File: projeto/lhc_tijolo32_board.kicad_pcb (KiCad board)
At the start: 2 copper layers, 25.4 x 64.8 mm, 49 parts, among them J1 USB_C_Receptacle_USB2.0, J2 OLED, J3 JTAG 10pin Connector, J4 Conn_01x20_Male, Q1 MMBT3904, Q2 MMBT3904, SW1 SW_Push, SW2 SW_Push, U1 AMS1117-3.3, U2 CH340G, U3 ESP32-WROOM-32D, Y1 12MHz 10ppm, Y2 32k 20ppm

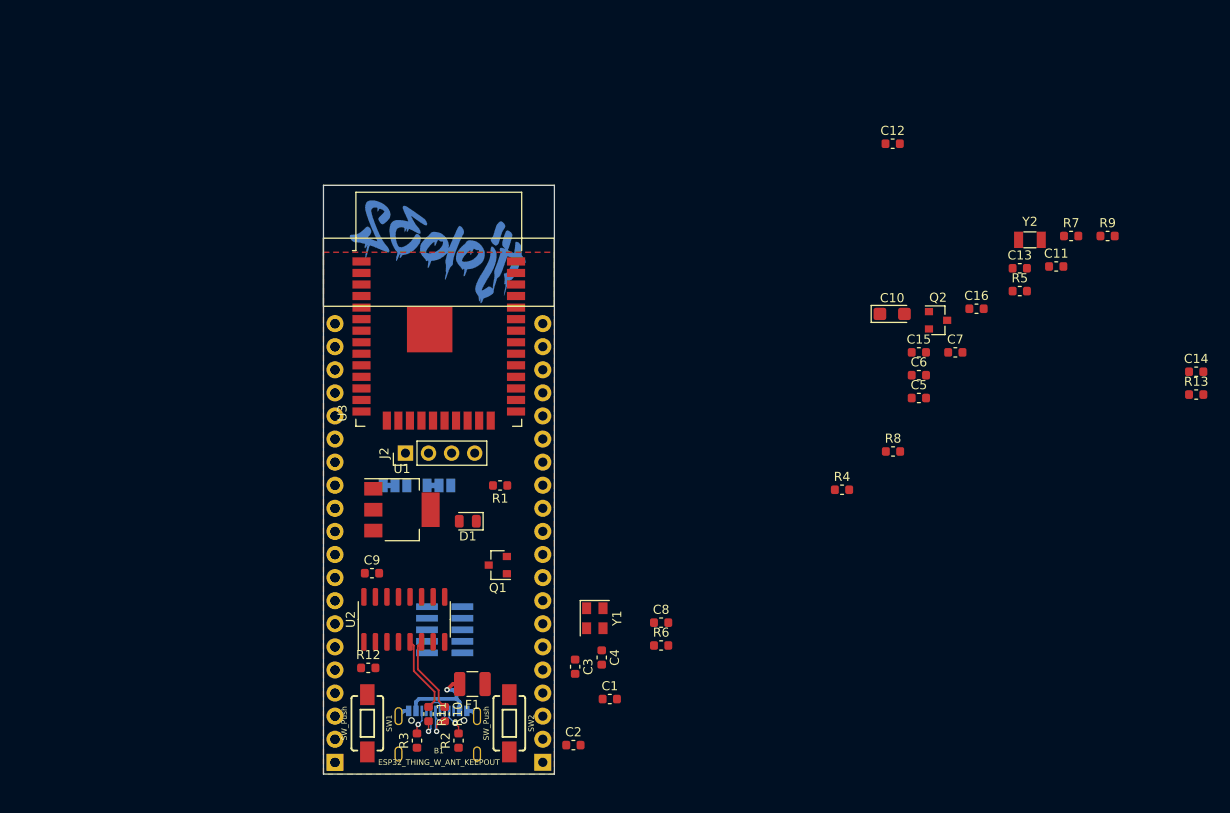
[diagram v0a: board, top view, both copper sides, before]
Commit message: Changed from Sparkfun to Adafruit Feather layout
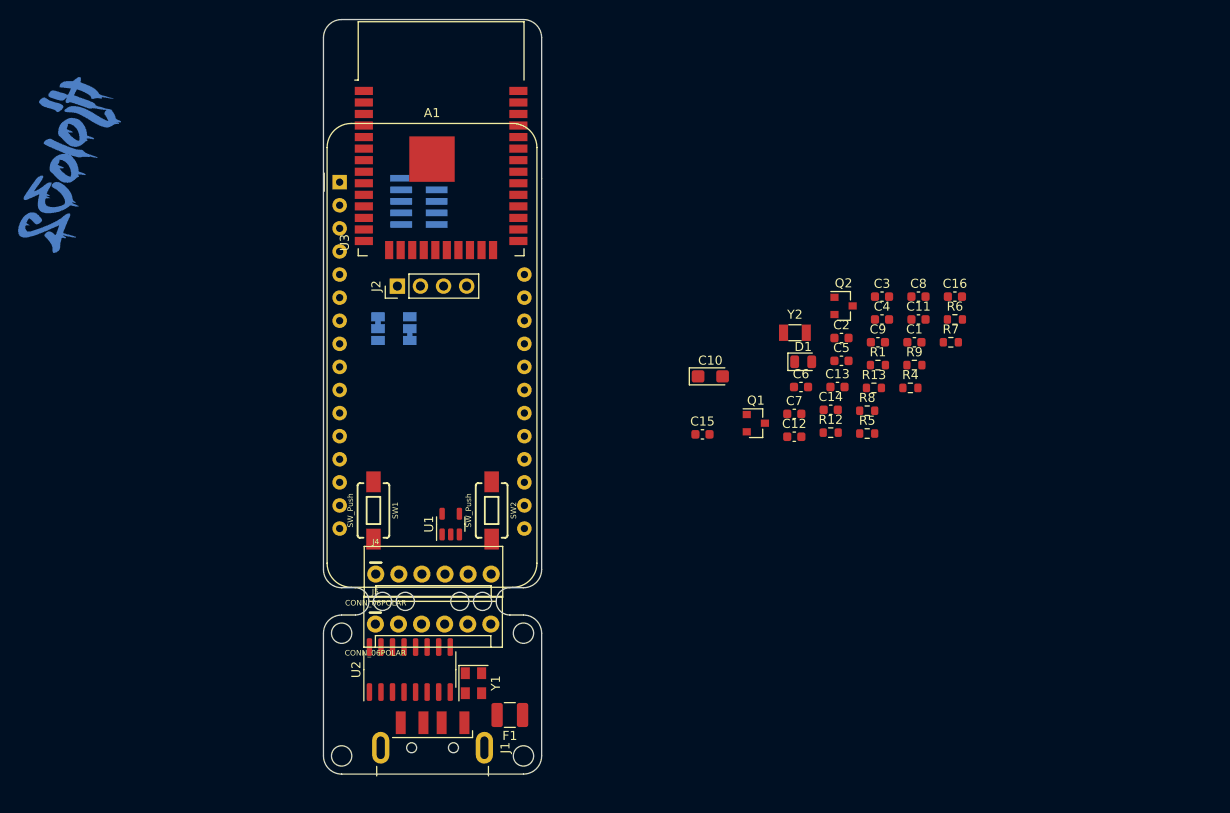
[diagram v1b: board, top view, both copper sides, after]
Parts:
- removed B1: ESP32_THING_W_ANT_KEEPOUT, Boards:ESP32_THING
- removed R10, R11: 0R, Resistor_SMD:R_0603_1608Metric
- removed R2, R3: 5k1R, Resistor_SMD:R_0603_1608Metric
- added A1: Adafruit_Feather_Generic, Module:Adafruit_Feather, F.Cu at (103.4, 45.4)
- added J5: CONN_06POLAR, Connectors:MOLEX-1X6, F.Cu at (107.3, 94.0)
- J1: value USB_C_Receptacle_USB2.0 -> USB_A; footprint Connector_USB:USB_C_Receptacle_Palconn_UTC16-G -> Connector_USB:USB_A_CNCTech_1001-011-01101_Horizontal; moved to F.Cu
- J4: value Conn_01x20_Male -> CONN_06POLAR; footprint Connector_PinHeader_2.54mm:PinHeader_1x20_P2.54mm_Vertical -> Connectors:MOLEX-1X6; moved to F.Cu
- U1: value AMS1117-3.3 -> AP2112K-3.3; footprint Package_TO_SOT_SMD:SOT-223-3_TabPin2 -> Package_TO_SOT_SMD:SOT-23-5
- moved C9 61.2 mm to (162.6, 63.0)
- moved R12 57.1 mm to (157.4, 72.9)
- moved C2 53.6 mm to (158.6, 62.5)
- moved C3 52.9 mm to (163.0, 58.0), turned to 0 degrees
- moved C1 51.6 mm to (166.6, 63.0)
- moved C4 48.3 mm to (163.0, 60.5), turned to 0 degrees
- moved R6 48.3 mm to (171.1, 60.5)
- moved J3 47.2 mm to (112.1, 47.5), turned to 180 degrees
- moved C8 45.7 mm to (167.1, 58.0)
- moved R1 43.6 mm to (162.6, 65.5), turned to 0 degrees
- moved G*** 41.7 mm to (73.6, 43.5), turned to 270 degrees (x2)
- moved D1 40.9 mm to (154.4, 65.1), turned to 0 degrees
- moved C14 40.4 mm to (157.4, 70.4)
- moved R13 35.5 mm to (162.2, 68.0)
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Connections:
- J4 pad 1: Net-(J4-Pad1) -> 5V
- J4 pad 2: Net-(J4-Pad2) -> ESP_RX
- J4 pad 3: Net-(J4-Pad3) -> ESP_TX
- J4 pad 4: Net-(J4-Pad4) -> DTR
- J4 pad 5: Net-(J4-Pad5) -> RTS
- J4 pad 6: Net-(J4-Pad6) -> GND
- U1 pad 1: GND -> 5V
- U1 pad 2: +3V3 -> GND
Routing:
- net Net-(F1-Pad2): track 10.5 -> 0.00 mm, vias 1 -> 0
- net D-: track 8.54 -> 0.00 mm
- net D+: track 8.54 -> 0.00 mm
- net Net-(J1-PadA7): track 6.75 -> 0.00 mm, vias 1 -> 0
- net Net-(J1-PadA6): track 6.10 -> 0.00 mm, vias 1 -> 0
- net Net-(J1-PadA5): track 2.93 -> 0.00 mm, vias 1 -> 0
- net GND: track 2.72 -> 0.00 mm
- net Net-(J1-PadB5): track 2.71 -> 0.00 mm, vias 1 -> 0
- removed copper zone on F.Cu, net GND
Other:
- board size 25.4 x 64.8 mm -> 24 x 83 mm

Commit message: Layout updated and added new 3d images
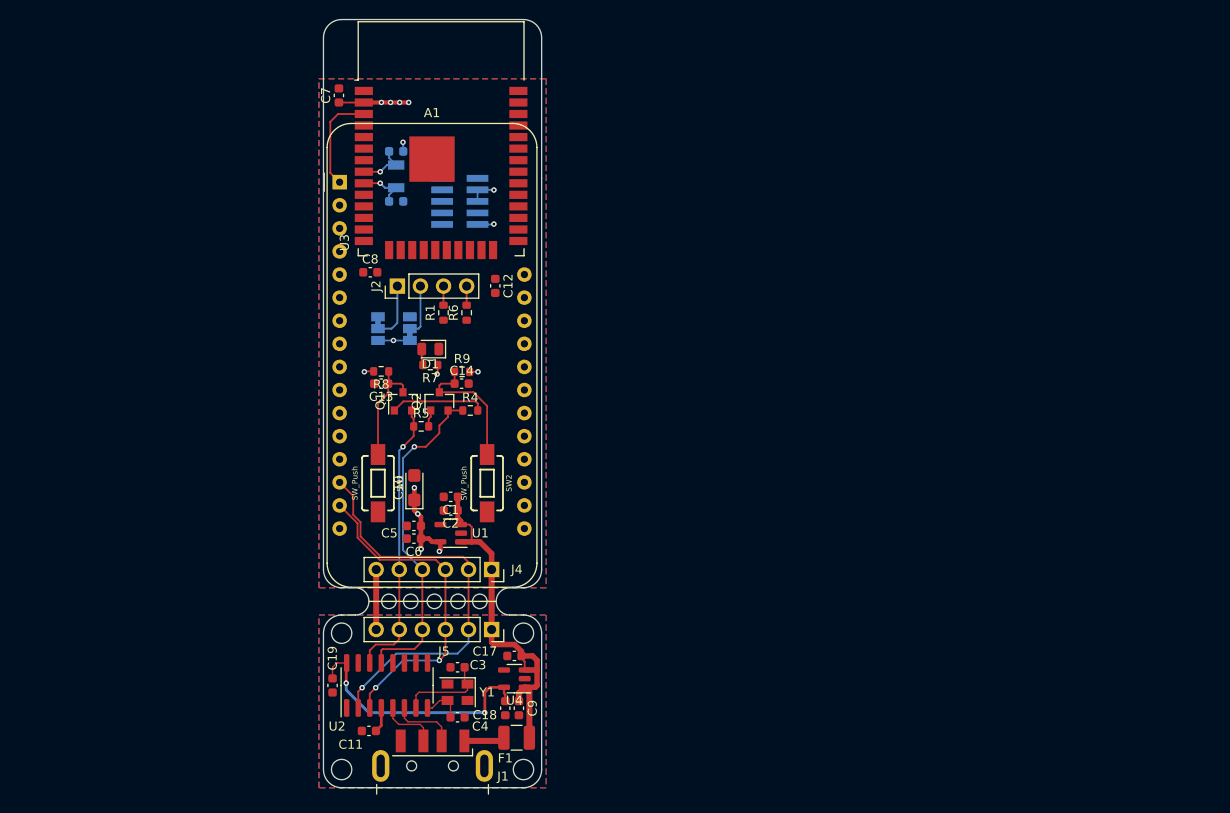
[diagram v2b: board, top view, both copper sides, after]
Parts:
- removed G***: LOGO, lhc_logos:tijolo32_medium_mask
- removed G***: LOGO, lhc_logos:tijolo32_medium_cu
- removed R12, R13: 0R, Resistor_SMD:R_0603_1608Metric
- added C17: 100nF, Capacitor_SMD:C_0603_1608Metric, F.Cu at (122.6, 97.5)
- added C18: 1uF, Capacitor_SMD:C_0603_1608Metric, F.Cu at (121.6, 103.2)
- added C19: 100nF, Capacitor_SMD:C_0603_1608Metric, F.Cu at (102.6, 100.7)
- added U4: AP2112K-3.3, Package_TO_SOT_SMD:SOT-23-5, F.Cu at (122.6, 100.0)
- C15, C16, Y2: moved to B.Cu
- C9: value 100nF -> 1uF
- J4, J5: footprint Connectors:MOLEX-1X6 -> Connector_PinSocket_2.54mm:PinSocket_1x06_P2.54mm_Vertical
- moved C11 75.5 mm to (106.6, 105.7), turned to 180 degrees
- moved C4 64.0 mm to (116.3, 104.2), turned to 180 degrees
- moved C16 62.3 mm to (109.6, 47.5)
- moved C3 62.0 mm to (116.3, 98.7), turned to 180 degrees
- moved C7 61.1 mm to (103.3, 35.8), turned to 90 degrees
- moved C8 60.4 mm to (106.8, 55.3)
- moved R7 57.3 mm to (113.3, 65.5), turned to 180 degrees
- moved C9 56.4 mm to (123.1, 103.2), turned to 270 degrees
- moved C1 53.8 mm to (115.6, 80.0), turned to 180 degrees
- moved R6 53.7 mm to (117.3, 59.7), turned to 90 degrees
- moved R8 53.6 mm to (108.0, 66.2), turned to 180 degrees
- moved C5 50.4 mm to (111.5, 83.2), turned to 180 degrees
- moved C13 50.2 mm to (108.0, 67.5), turned to 180 degrees
- moved R9 49.8 mm to (116.8, 66.2)
- moved R5 49.1 mm to (112.3, 72.2)
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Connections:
- C3 pad 1: Net-(C3-Pad1) -> XI
- C4 pad 2: Net-(C4-Pad2) -> XO
- C9 pad 1: +3V3 -> 5V
- U2 pad 16: +3V3 -> Net-(C18-Pad1)
- U2 pad 2: Net-(R12-Pad2) -> ESP_RX
- U2 pad 3: Net-(R13-Pad1) -> ESP_TX
- Y1 pad 2: Net-(C4-Pad2) -> GND
- Y1 pad 4: Net-(C3-Pad1) -> GND
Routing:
- net ESP_RX: track 0.00 -> 45.0 mm, vias 0 -> 1
- net 5V: track 0.00 -> 40.7 mm
- net DTR: track 0.00 -> 37.0 mm, vias 0 -> 1
- net ESP_TX: track 0.00 -> 36.5 mm, vias 0 -> 2
- net RTS: track 0.00 -> 31.0 mm, vias 0 -> 1
- net Net-(C18-Pad1): track 0.00 -> 28.4 mm, vias 0 -> 2
- net ESP_RST: track 0.00 -> 23.2 mm
- net +3V3: track 0.00 -> 21.1 mm, vias 0 -> 11
- net GND: track 0.00 -> 16.0 mm, vias 0 -> 4
- net ESP_BOOT: track 0.00 -> 15.0 mm
- net Net-(Q1-Pad1): track 0.00 -> 10.5 mm
- net XI: track 0.00 -> 9.95 mm
- net D-: track 0.00 -> 7.17 mm
- net OLED_P1: track 0.00 -> 6.44 mm
- net D+: track 0.00 -> 6.40 mm
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- added copper zone on B.Cu, net +3V3
- added copper zone on B.Cu, net GND
- added copper zone on F.Cu, net GND
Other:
- board size 24 x 83 mm -> 24 x 84.5 mm

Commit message: Layout updated
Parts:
- moved D1 13.3 mm to (114.3, 77.0), turned to 270 degrees
- moved R7 11.8 mm to (116.1, 77.0), turned to 270 degrees
- moved JP1 5.70 mm to (116.6, 63.0), turned to 180 degrees
- moved JP2 4.51 mm to (111.8, 63.0), turned to 0 degrees
- moved C8 0.45 mm to (106.3, 55.5)
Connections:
- U3 pad 27: IO16 -> SDA
- U3 pad 28: IO17 -> SCL
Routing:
- net SVN: track 0.00 -> 32.2 mm, vias 0 -> 1
- net SVP: track 0.00 -> 31.8 mm, vias 0 -> 1
- net IO27: track 0.00 -> 30.6 mm
- net IO26: track 0.00 -> 29.8 mm
- net IO25: track 0.00 -> 27.9 mm, vias 0 -> 1
- net IO35: track 0.00 -> 26.6 mm, vias 0 -> 1
- net IO34: track 0.00 -> 22.5 mm, vias 0 -> 1
- net SCL: track 2.11 -> 18.7 mm, vias 0 -> 1
- net IO33-32kXN: track 5.59 -> 21.8 mm, vias 1 -> 2
- net IO14-MTMS: track 0.00 -> 15.1 mm, vias 0 -> 1
- net SDA: track 2.10 -> 17.1 mm, vias 0 -> 1
- net IO12-MTDI: track 0.00 -> 13.6 mm, vias 0 -> 3
- net ESP_BOOT: track 15.0 -> 28.5 mm
- net IO13-MTCK: track 0.00 -> 9.56 mm, vias 0 -> 1
- net IO15-MTDO: track 0.00 -> 8.99 mm, vias 0 -> 1
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
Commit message: Layout improved
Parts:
- added G***: LOGO, lhc_logos:lhc_logo_alt_small, B.Cu at (113.6, 103.0)
- moved C8 1.87 mm to (108.1, 54.9), turned to 180 degrees
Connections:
- A1 pad 10: SVN -> IO26
- A1 pad 11: IO25 -> Net-(A1-Pad11)
- A1 pad 12: IO26 -> Net-(A1-Pad12)
- A1 pad 13: IO27 -> Net-(A1-Pad13)
- A1 pad 16: IO23 -> Net-(A1-Pad16)
- A1 pad 20: IO4 -> IO22
- A1 pad 21: IO5 -> IO21
- A1 pad 22: IO18 -> IO19
- A1 pad 23: IO19 -> IO18
- A1 pad 24: IO21 -> IO5
- A1 pad 25: IO22 -> IO4
- A1 pad 28: Net-(A1-Pad28) -> IO23
- A1 pad 3: Net-(A1-Pad3) -> IO27
- A1 pad 5: IO32-32kXP -> SVP
- A1 pad 6: IO33-32kXN -> SVN
- A1 pad 9: SVP -> IO25
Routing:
- net ESP_TX: track 36.5 -> 85.1 mm, vias 2 -> 6
- net IO22: track 0.00 -> 40.1 mm, vias 0 -> 1
- net ESP_RST: track 23.2 -> 58.7 mm, vias 0 -> 4
- net IO21: track 0.00 -> 33.5 mm, vias 0 -> 1
- net SDA: track 17.1 -> 47.6 mm, vias 1 -> 2
- net SCL: track 18.7 -> 47.3 mm, vias 1 -> 2
- net IO19: track 0.00 -> 28.2 mm, vias 0 -> 1
- net IO2: track 0.00 -> 27.0 mm, vias 0 -> 1
- net IO27: track 30.6 -> 3.90 mm
- net 5V: track 40.7 -> 65.1 mm, vias 0 -> 4
- net IO18: track 0.00 -> 24.2 mm, vias 0 -> 1
- net IO23: track 0.00 -> 21.0 mm
- net IO5: track 0.00 -> 20.1 mm, vias 0 -> 1
- net IO33-32kXN: track 21.8 -> 5.58 mm, vias 2 -> 1
- net SVP: track 31.8 -> 17.5 mm
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
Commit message: Layout LIVE
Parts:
- removed the G*** at (113.6, 103.0)
- added ?: , Aesthetics:OSHW-LOGO-M, B.Cu at (122.7, 106.6)
- added ?: , Aesthetics:OSHW-LOGO-L, F.Cu at (108.4, 62.3)
- added G***: LOGO, lhc_logos:lhc_logo_alt_xlarge, B.Cu at (113.7, 33.5)
- added G***: LOGO, lhc_logos:lhc_logo_alt_large, B.Cu at (113.7, 100.3)
- JP1, JP2: footprint Jumper:SolderJumper-3_P1.3mm_Bridged12_Pad1.0x1.5mm_NumberLabels -> Jumper:SolderJumper-3_P1.3mm_Open_Pad1.0x1.5mm_NumberLabels
- moved JP2 0.09 mm to (111.8, 63.0)
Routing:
- net ESP_RX: track 38.7 -> 98.4 mm, vias 3 -> 5
- net ESP_TX: track 85.1 -> 92.1 mm, vias 6 -> 5
- net IO12-MTDI: track 11.4 -> 10.5 mm, vias 3 -> 1
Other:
- board text added: "3V3"
- board text added: "GND"
- board text added: "IO16"
- board text added: "IO17"
- board text added: "IO23"
- board text added: "LHC"

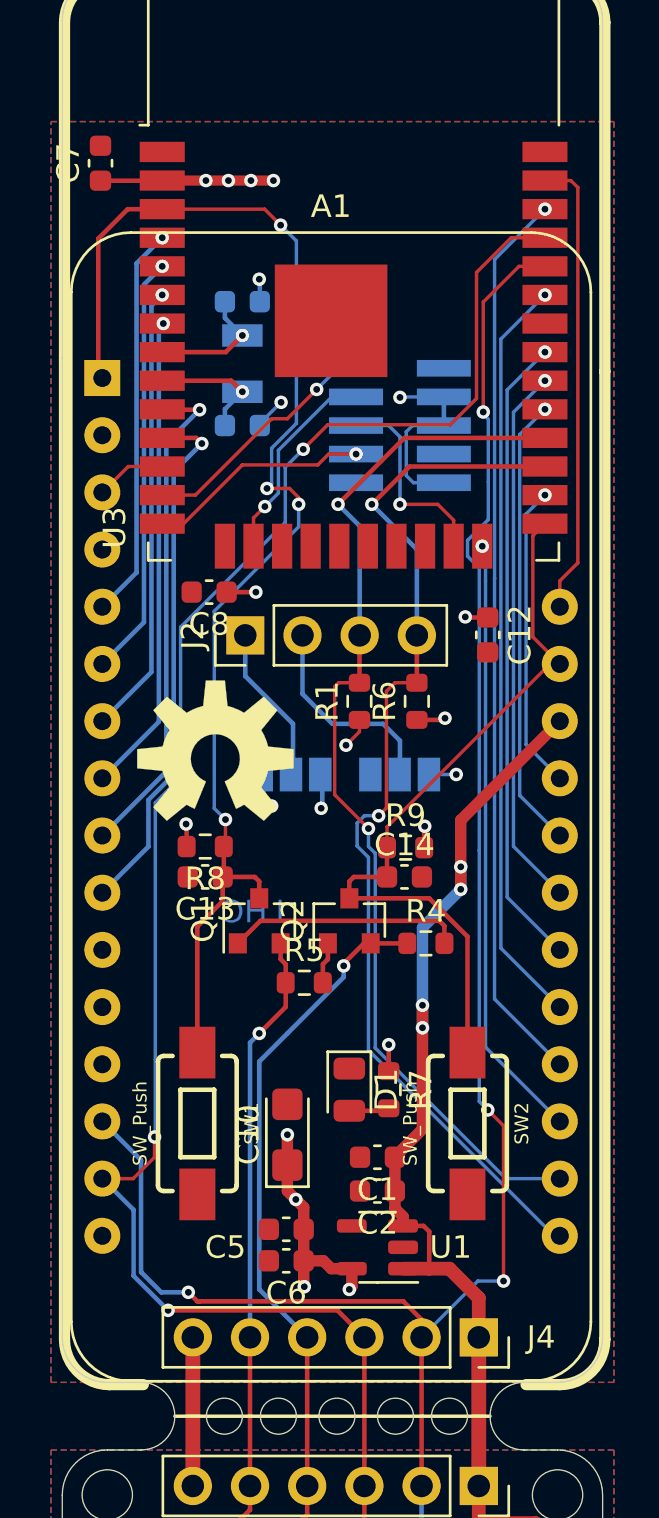
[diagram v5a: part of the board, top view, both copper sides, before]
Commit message: Updated silk on both sides
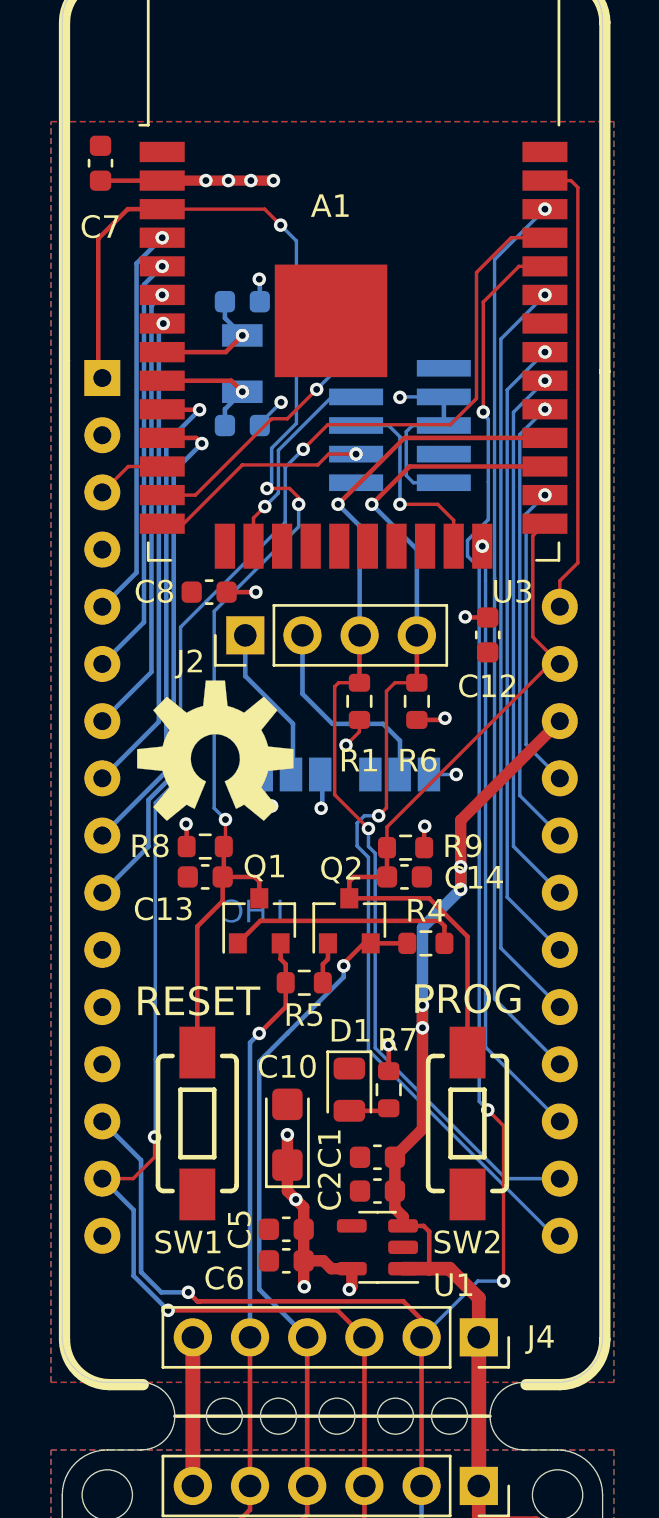
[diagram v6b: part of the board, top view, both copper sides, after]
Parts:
- removed the G*** at (113.7, 100.3)
- added G***: LOGO, lhc_logos:lhc_logo_alt_small, B.Cu at (118.0, 103.1)
- moved ? 16.2 mm to (106.9, 103.2)
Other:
- board text added: "1"
- board text added: "5V0"
- board text added: "9"
- board text added: "DEBUG"
- board text added: "DTR"
- board text added: "IO0"
- board text added: "IO02"
- board text added: "IO04"
- board text added: "IO05"
- board text added: "IO18"
- board text added: "IO19"
- board text added: "IO21"
- board text added: "IO22"
- board text added: "IO25"
- board text added: "IO26"
- board text added: "IO27"
- board text added: "IO34"
- board text added: "IO35"
- board text added: "PROG"
- board text added: "RESET"
- board text added: "RST"
- board text added: "RTS"
- board text added: "RX"
- board text added: "SVN"
- board text added: "SVP"
- board text added: "TX"
